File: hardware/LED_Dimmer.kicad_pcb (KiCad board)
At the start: 2 copper layers, 50 x 49 mm, 26 parts, among them J1 Molex PicoBlade 53261-0871 1x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, Q1 2N7002K-7, Q2 2N7002K-7, Q3 2N7002K-7, SW1 N/A, SW2 N/A, U1 BGM220P, U2 L78L33A

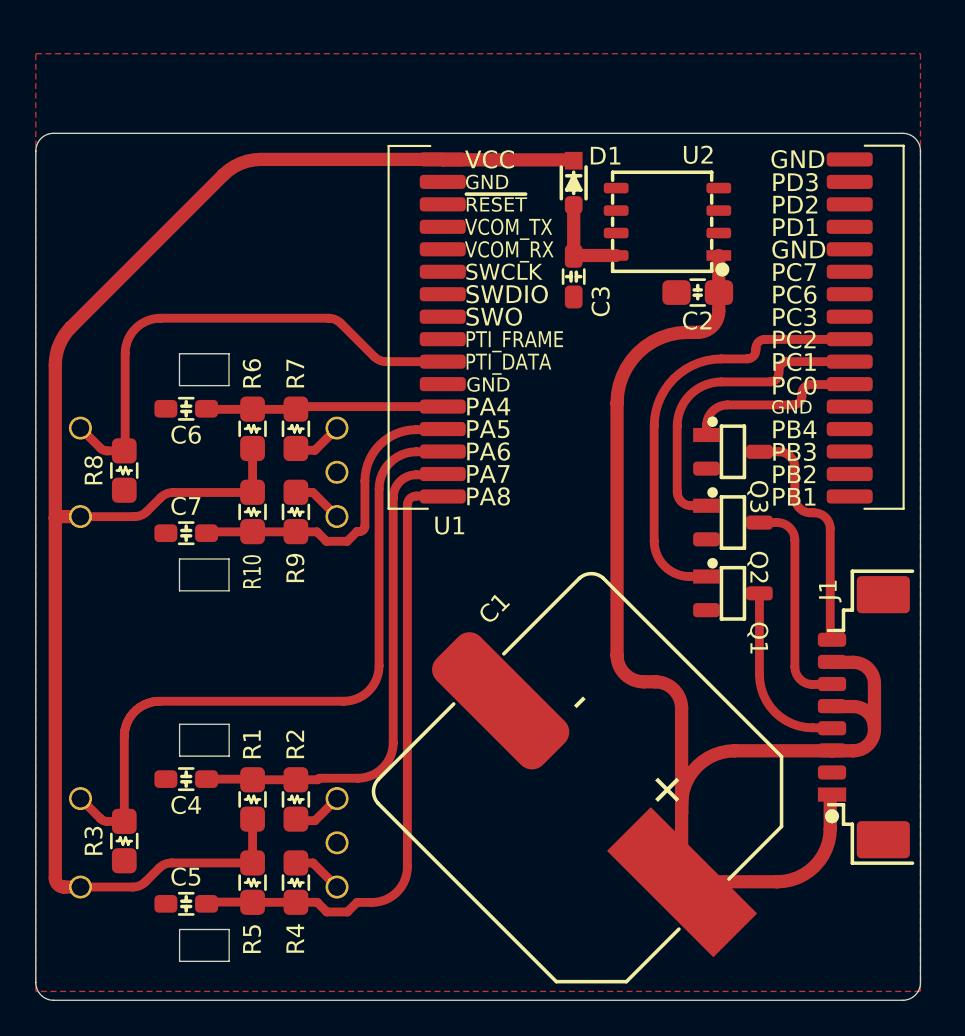
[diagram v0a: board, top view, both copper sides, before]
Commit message: v2 Board Ready - Added Art - Removed DRC/ERC - Finished BOM
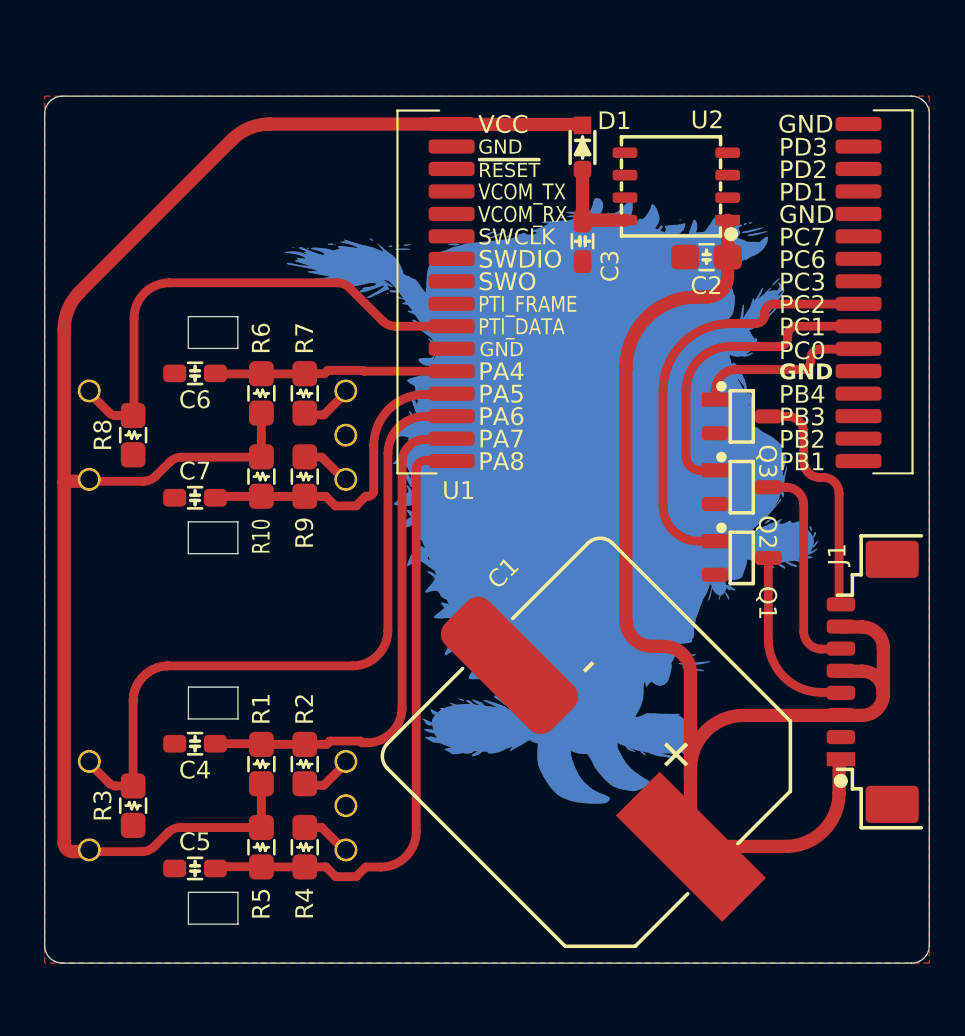
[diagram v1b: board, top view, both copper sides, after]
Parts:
- added G1: PCB Art, Gruffalo_Dimmer:Gruffalo_Art, B.Cu at (88.5, 115.5)
- moved SW1 2.16 mm to (84.5, 115.6)
- moved SW2 2.16 mm to (84.5, 94.7)
- moved C1 2.06 mm to (106.4, 112.8)
- moved C2 2.06 mm to (112.4, 84.6)
- moved C3 2.06 mm to (105.4, 83.7)
- moved C4 2.06 mm to (83.5, 112.1)
- moved C5 2.06 mm to (83.5, 119.2)
- moved C6 2.06 mm to (83.5, 91.2)
- moved C7 2.06 mm to (83.5, 98.2)
- moved D1 2.06 mm to (105.4, 78.4)
- moved J1 2.06 mm to (122.9, 108.6)
- moved Q1 2.06 mm to (114.4, 101.6)
- moved Q2 2.06 mm to (114.4, 97.6)
- moved Q3 2.06 mm to (114.4, 93.6)
- moved R1 2.06 mm to (87.2, 113.2)
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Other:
- board text added: "Para Ari y Maia, Sweet dreams. Marzo 2023"
- board text removed: "Para Ari, Sweet dreams. Mayo 2020"

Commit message: Getting ready for KiBot. Removed some old references to 3D models from some parts
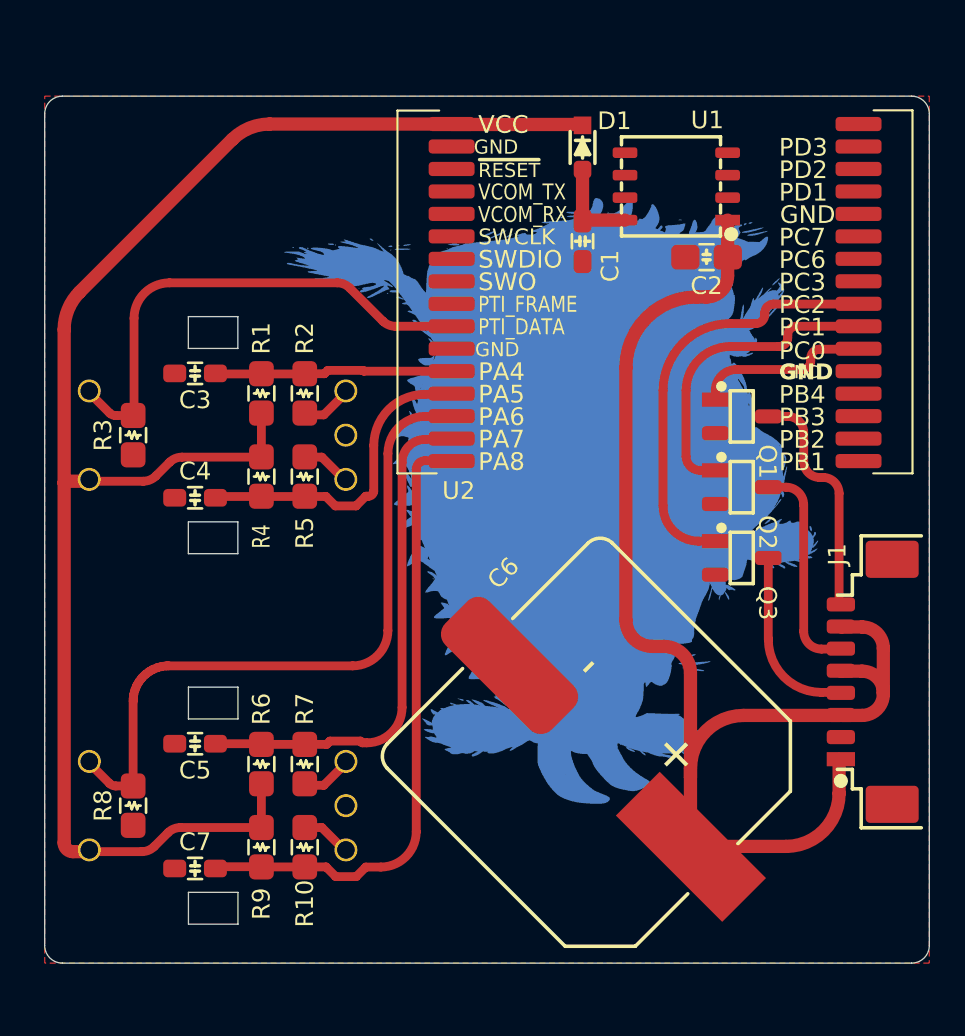
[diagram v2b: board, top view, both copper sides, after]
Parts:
- renumbered C3 to C1, C6 to C3, C7 to C4, C4 to C5, C1 to C6, C5 to C7, G1 to G101, Q3 to Q1, Q1 to Q3, R6 to R1, R4 to R10, R7 to R2, R8 to R3, R10 to R4, R9 to R5, R1 to R6, R2 to R7, R3 to R8, R5 to R9, SW2 to SW101, SW1 to SW102, U2 to U1, U1 to U2
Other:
- rule pad_to_mask_clearance: 0.05 -> 0

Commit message: Changed the 3D model of the diode to an externally-added STEP file Removed Refs from potentiometers
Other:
- board text added: "Layer Intentionally left empty"
- board text added: "PCB3D_BR_BOARD"
- board text added: "PCB3D_TL_BOARD"

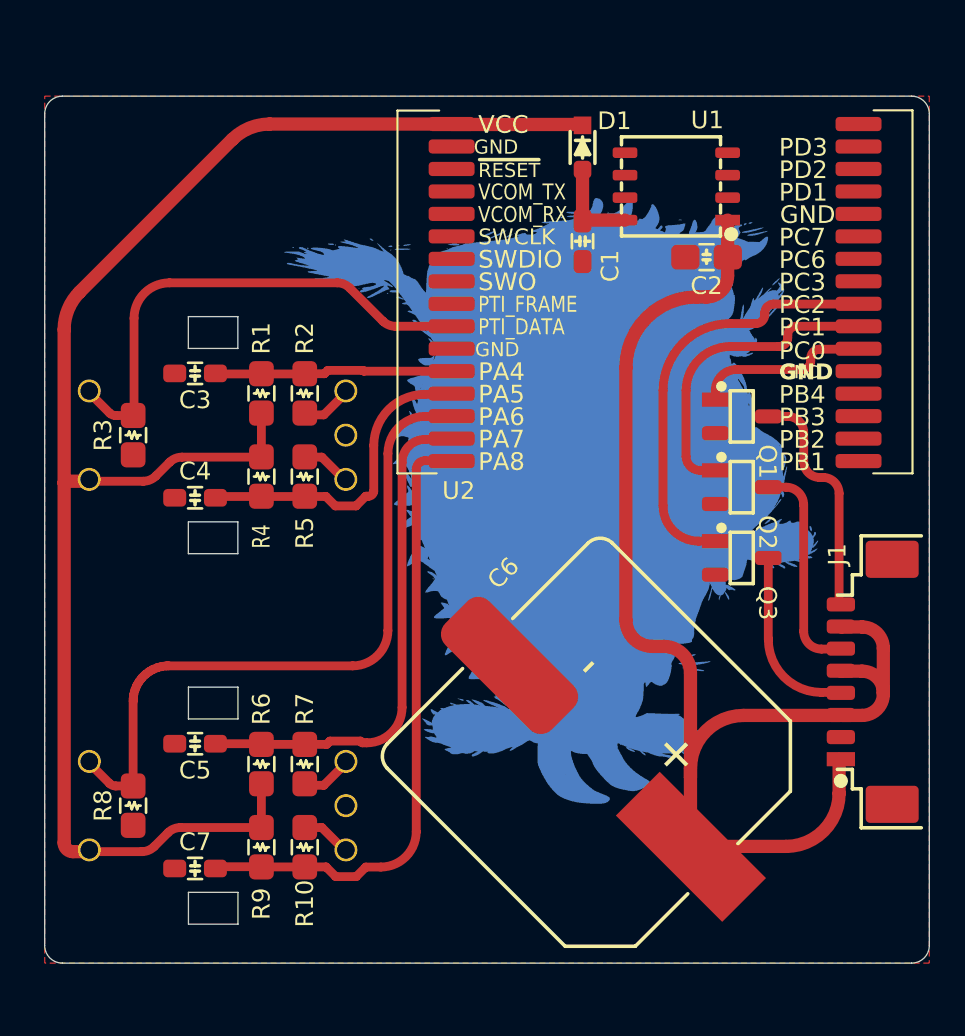
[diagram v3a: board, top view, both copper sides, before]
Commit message: Not sure of the complete list of changes, but fixed a bunch of DRC/ERC errors
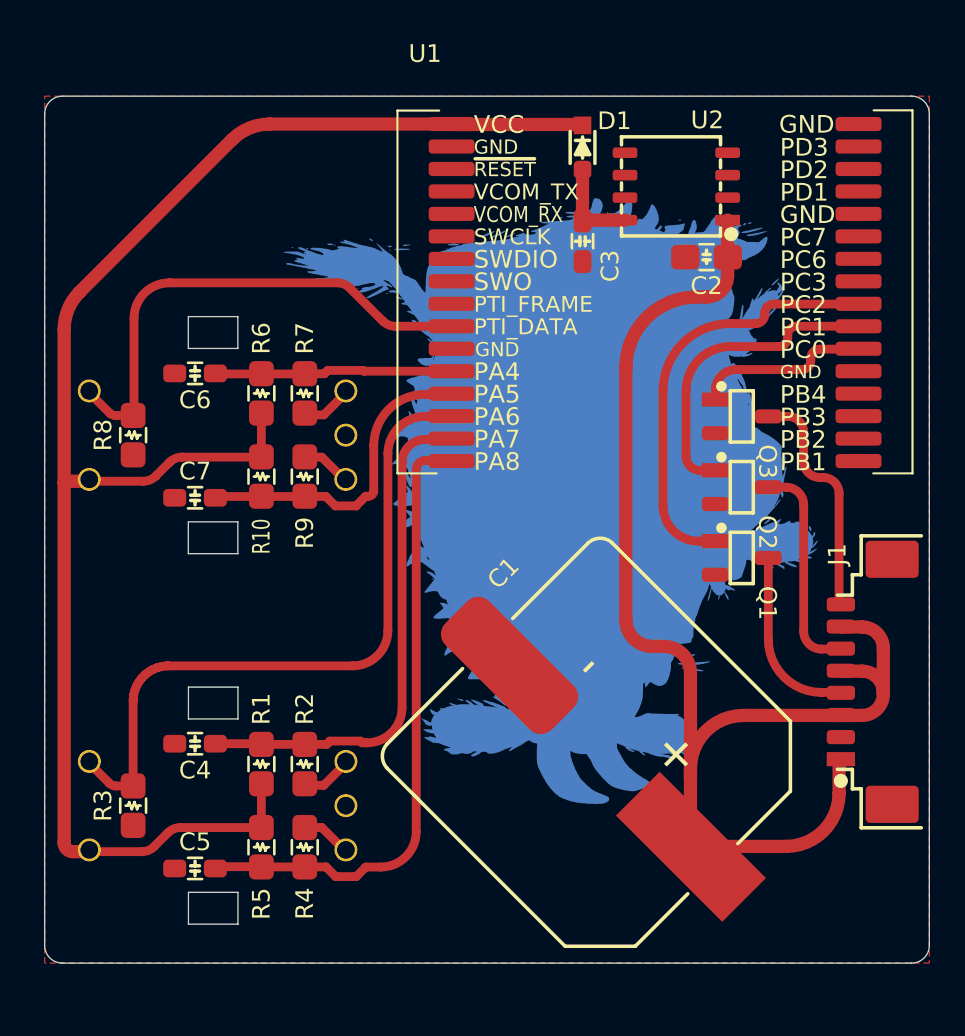
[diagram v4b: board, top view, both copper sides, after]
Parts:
- renumbered C6 to C1, C1 to C3, C5 to C4, C7 to C5, C3 to C6, C4 to C7, G101 to G1, Q3 to Q1, Q1 to Q3, R6 to R1, R4 to R10, R7 to R2, R8 to R3, R10 to R4, R9 to R5, R1 to R6, R2 to R7, R3 to R8, R5 to R9, SW102 to SW1, SW101 to SW2, U2 to U1, U1 to U2
